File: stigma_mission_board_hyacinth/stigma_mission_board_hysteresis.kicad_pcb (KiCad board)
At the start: 4 copper layers, 50 x 150 mm, 207 parts, among them J1 Conn_02x04_Top_Bottom, J10 Conn_02x02_Top_Bottom, J11 Conn_02x02_Top_Bottom, J12 Conn_02x02_Top_Bottom, J13 Conn_02x02_Top_Bottom, J2 Conn_02x05_Top_Bottom_Mountin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, J3 Conn_02x04_Top_Bottom, J7 JST-GH 4Pin, J8 SMA, J9 SMA, Q1 DMN2056U, Q2 DMN2056U, Q3 AOSP21321, Q4 DMN2056U, Q5 AOSP21321, Q6 DMN2056U, Q7 AOSP21321, Q8 DMN2056U, Q9 AOSP21321, U1 L7805, U10 MCP2562-E-SN, U11 LAN8742A, U12 Ai-Thinker-Ra-01, U13 INA181, U14 INA181, U15 INA181, U16 INA181, U2 SN74HCS594, U3 L7805, U4 AZ1117H-ADJ, U5 INA181, U6 AZ1117H-ADJ, U7 MCP2562-E-SN, U8 Ai-Thinker-Ra-01, U9 TPD4E1U06, Y1 25MHz

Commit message: some tydiing up and adding footprints
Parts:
- added R59: 10k, Resistor_SMD:R_0603_1608Metric, F.Cu at (159.2, 130.5)
- added R60: 1k, Resistor_SMD:R_0603_1608Metric, F.Cu at (159.2, 133.0)
- JP3, JP4, JP5, JP6: footprint Jumper:SolderJumper-3_Open_RoundedPad2x2mm -> stigma:SolderJumper-3_Open_RoundedPad2x2mm
- R10: value 310R -> 100k; footprint Resistor_SMD:R_0402_1005Metric -> Resistor_SMD:R_0603_1608Metric
- R11: value 10k -> 220
- R12: value 10k -> 310R; footprint Resistor_SMD:R_0603_1608Metric -> Resistor_SMD:R_0402_1005Metric
- R14: value 150R -> 10k
- R15: value 220 -> 10k
- R16: value 310R -> 150R; footprint Resistor_SMD:R_0402_1005Metric -> Resistor_SMD:R_0603_1608Metric
- R17: value 0 -> 220; footprint Resistor_SMD:R_0402_1005Metric -> Resistor_SMD:R_0603_1608Metric
- R18: value 0 -> 310R
- R19: value 120, DNP -> 0; footprint Resistor_SMD:R_0603_1608Metric -> Resistor_SMD:R_0402_1005Metric
- R20: footprint Resistor_SMD:R_0603_1608Metric -> Resistor_SMD:R_0402_1005Metric
- R21: value 10k -> 120, DNP
- R22: value 1k5 -> 0
- R24: value 10k -> 1k5
- R26: value 120, DNP -> 10k
- R27: value 50R -> 10k
- R28: value 50R -> 120, DNP
- R31: value 0 -> 50R
- R32: value 33R -> 50R
- R33, R38: value 33R -> 0
- R34: value 10k -> 33R
- R36: value 0 -> 10k
- R37: value 12.1k -> 33R
- R39: value 10k -> 12.1k
- R4: value 150R -> 100k
- R40: value 270 -> 33R
- R41: value 270 -> 10k
- R42: value 10k -> 270
- R43: value 60R -> 270
- R44: value 1k -> 10k
- R45, R49, R53, R57: value 10k -> 60R
- R47, R51, R55: value 60R -> 10k
- R5: value @todo -> 10k
- R6: value 100mR 1% -> 150R; footprint Resistor_SMD:R_Shunt_Ohmite_LVK12 -> Resistor_SMD:R_0603_1608Metric
- R7: value 100k -> @todo
- R8: value 100k -> 100mR 1%; footprint Resistor_SMD:R_0603_1608Metric -> Resistor_SMD:R_Shunt_Ohmite_LVK12
- R9: value 220 -> 100k
- moved R40 241.0 mm to (273.9, 118.8)
- moved R42 241.0 mm to (273.9, 116.3)
- moved R41 231.3 mm to (274.0, 123.6)
- moved R17 205.6 mm to (272.2, 139.6)
- moved D14 191.2 mm to (193.0, 182.5)
- moved JP2 191.2 mm to (187.9, 179.7)
- moved JP3 186.4 mm to (152.0, 254.9)
- moved Q2 183.9 mm to (148.1, 269.2)
- moved R43 183.9 mm to (159.9, 261.2)
- moved U13 183.9 mm to (148.3, 264.5)
- moved C44 183.9 mm to (159.9, 251.2)
- moved D17 183.9 mm to (153.8, 269.0)
- moved D18 183.9 mm to (152.9, 266.0)
- moved D19 183.9 mm to (152.9, 263.4)
- moved Q3 183.9 mm to (166.1, 250.8)
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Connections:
- J4 pad 29: @TODO Free-ADC -> ADC_HIGH_CURRENT2
- R10 pad 1: Net-(U4-GND) -> high_current
- R10 pad 2: GND -> ADC_HIGH_CURRENT
- R11 pad 1: BUZZER -> Net-(D12-A)
- R11 pad 2: GND -> Net-(D13-A)
- R12 pad 1: ADC_MAIN_VOLTAGE -> Net-(U4-GND)
- R13 pad 1: ADC_HIGH_CURRENT -> BUZZER
- R14 pad 1: Net-(D15-A) -> ADC_MAIN_VOLTAGE
- R14 pad 2: Net-(U6-GND) -> GND
- R15 pad 1: Net-(D15-A) -> ADC_HIGH_CURRENT
- R15 pad 2: Net-(D16-A) -> GND
- R16 pad 1: Net-(U6-GND) -> Net-(D15-A)
- R16 pad 2: GND -> Net-(U6-GND)
- R17 pad 1: HSE_IN -> Net-(D15-A)
- R17 pad 2: Net-(C31-Pad2) -> Net-(D16-A)
- R18 pad 1: Net-(C32-Pad2) -> Net-(U6-GND)
- R18 pad 2: HSE_OUT -> GND
- R19 pad 1: CAN_1_H -> HSE_IN
- R19 pad 2: CAN_1_L -> Net-(C31-Pad2)
- R20 pad 1: Net-(U8-ANT) -> Net-(C32-Pad2)
- R20 pad 2: Net-(J8-In) -> HSE_OUT
- R21 pad 1: SR_ETH_RESET -> CAN_1_H
- R21 pad 2: +3.3V -> CAN_1_L
- R22 pad 1: Net-(U11-MDIO) -> Net-(U8-ANT)
- R22 pad 2: +3.3V -> Net-(J8-In)
- R23 pad 1: Net-(U11-CRS_DV/MODE2) -> SR_ETH_RESET
- R24 pad 1: Net-(U11-RXD1/MODE1) -> Net-(U11-MDIO)
- R25 pad 1: Net-(U11-RXD0/MODE0) -> Net-(U11-CRS_DV/MODE2)
- R26 pad 1: CAN_2_H -> Net-(U11-RXD1/MODE1)
- R26 pad 2: CAN_2_L -> +3.3V
- R27 pad 1: Net-(U11-VDD1A) -> Net-(U11-RXD0/MODE0)
- R27 pad 2: /TXP -> +3.3V
- R28 pad 1: Net-(U11-VDD1A) -> CAN_2_H
- R28 pad 2: /TXN -> CAN_2_L
- R29 pad 2: /RXP -> /TXP
- R30 pad 2: /RXN -> /TXN
- R31 pad 1: Net-(U12-ANT) -> Net-(U11-VDD1A)
- R31 pad 2: Net-(J9-In) -> /RXP
- R32 pad 1: Net-(U11-RXD0/MODE0) -> Net-(U11-VDD1A)
- R32 pad 2: ETH_RXD0 -> /RXN
- R33 pad 1: Net-(U11-RXD1/MODE1) -> Net-(U12-ANT)
- R33 pad 2: ETH_RXD1 -> Net-(J9-In)
- R34 pad 1: Net-(U11-RXER/PHYAD0) -> Net-(U11-RXD0/MODE0)
- R34 pad 2: GND -> ETH_RXD0
- R35 pad 1: Net-(U11-CRS_DV/MODE2) -> Net-(U11-RXD1/MODE1)
- R35 pad 2: ETH_RMII_CRS_DV -> ETH_RXD1
- R36 pad 1: Net-(U11-MDIO) -> Net-(U11-RXER/PHYAD0)
- R36 pad 2: ETH_MDIO -> GND
- R37 pad 1: Net-(U11-RBIAS) -> Net-(U11-CRS_DV/MODE2)
- R37 pad 2: GND -> ETH_RMII_CRS_DV
- R38 pad 1: Net-(U11-~{INT}/REFCLKO) -> Net-(U11-MDIO)
- R38 pad 2: ETH_REF_CLK -> ETH_MDIO
- R39 pad 1: ETH_nINT -> Net-(U11-RBIAS)
- R4 pad 1: Net-(D12-A) -> high_current
- R4 pad 2: Net-(U4-GND) -> ADC_HIGH_CURRENT2
- R40 pad 1: Net-(RJ1-L-) -> Net-(U11-~{INT}/REFCLKO)
- R40 pad 2: GND -> ETH_REF_CLK
- R41 pad 1: Net-(RJ1-R+) -> ETH_nINT
- R42 pad 1: +3.3V -> Net-(RJ1-L-)
- R42 pad 2: ETH_nINT -> GND
- R43 pad 1: RECOVERY_3_CONT_CHECK -> Net-(RJ1-R+)
- R43 pad 2: Net-(U13-+) -> GND
- R44 pad 1: /Recovery Output3/high_current -> +3.3V
- R44 pad 2: Net-(Q2-D) -> ETH_nINT
- R45 pad 1: RECOVERY_3 -> RECOVERY_3_CONT_CHECK
- R45 pad 2: GND -> Net-(U13-+)
- R46 pad 1: /Recovery Output3/recovery_switched -> /Recovery Output3/high_current
- R46 pad 2: Net-(D19-A) -> Net-(Q2-D)
- R47 pad 1: RECOVERY_2_CONT_CHECK -> RECOVERY_3
- R47 pad 2: Net-(U14-+) -> GND
- R48 pad 1: /Recovery Output2/high_current -> /Recovery Output3/recovery_switched
- R48 pad 2: Net-(Q4-D) -> Net-(D19-A)
- R49 pad 1: RECOVERY_2 -> RECOVERY_2_CONT_CHECK
- R49 pad 2: GND -> Net-(U14-+)
- R5 pad 1: BUZZER -> ADC_HIGH_CURRENT2
- R5 pad 2: Net-(Q1-G) -> GND
- R50 pad 1: /Recovery Output2/recovery_switched -> /Recovery Output2/high_current
- R50 pad 2: Net-(D22-A) -> Net-(Q4-D)
- R51 pad 1: RECOVERY_4_CONT_CHECK -> RECOVERY_2
- R51 pad 2: Net-(U15-+) -> GND
- R52 pad 1: /Recovery Output 4/high_current -> /Recovery Output2/recovery_switched
- R52 pad 2: Net-(Q6-D) -> Net-(D22-A)
- R53 pad 1: RECOVERY_4 -> RECOVERY_4_CONT_CHECK
- R53 pad 2: GND -> Net-(U15-+)
- R54 pad 1: /Recovery Output 4/recovery_switched -> /Recovery Output 4/high_current
- R54 pad 2: Net-(D25-A) -> Net-(Q6-D)
- R55 pad 1: RECOVERY_1_CONT_CHECK -> RECOVERY_4
- R55 pad 2: Net-(U16-+) -> GND
- R56 pad 1: /Recovery Output 1/high_current -> /Recovery Output 4/recovery_switched
- R56 pad 2: Net-(Q8-D) -> Net-(D25-A)
- R57 pad 1: RECOVERY_1 -> RECOVERY_1_CONT_CHECK
- R57 pad 2: GND -> Net-(U16-+)
- R58 pad 1: /Recovery Output 1/recovery_switched -> /Recovery Output 1/high_current
- R58 pad 2: Net-(D28-A) -> Net-(Q8-D)
- R6 pad 1: v_main_pre_sense -> Net-(D12-A)
- R6 pad 2: Net-(U5-+) -> Net-(U4-GND)
- R7 pad 1: v_main_pre_sense -> BUZZER
- R7 pad 2: ADC_MAIN_VOLTAGE -> Net-(Q1-G)
- R8 pad 1: high_current -> v_main_pre_sense
- R8 pad 2: ADC_HIGH_CURRENT -> Net-(U5-+)
- R9 pad 1: Net-(D12-A) -> v_main_pre_sense
- R9 pad 2: Net-(D13-A) -> ADC_MAIN_VOLTAGE
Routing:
- net Net-(U15-+): vias 1 -> 0
- net GND: vias 24 -> 11
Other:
- board text added: "recovery1"
- board text added: "recovery2"
- board text added: "recovery3"
- board text added: "recovery4"
- board text added: "see what we do with those"
- board text removed: "50 x 200 mm"
- board text removed: "R1"
- board text removed: "R2"
- board text removed: "R3"
- board text removed: "R4"
- board text removed: "Recovery Power 1"
- board text removed: "Recovery Power 2"
- board text removed: "Vehicle BUS"

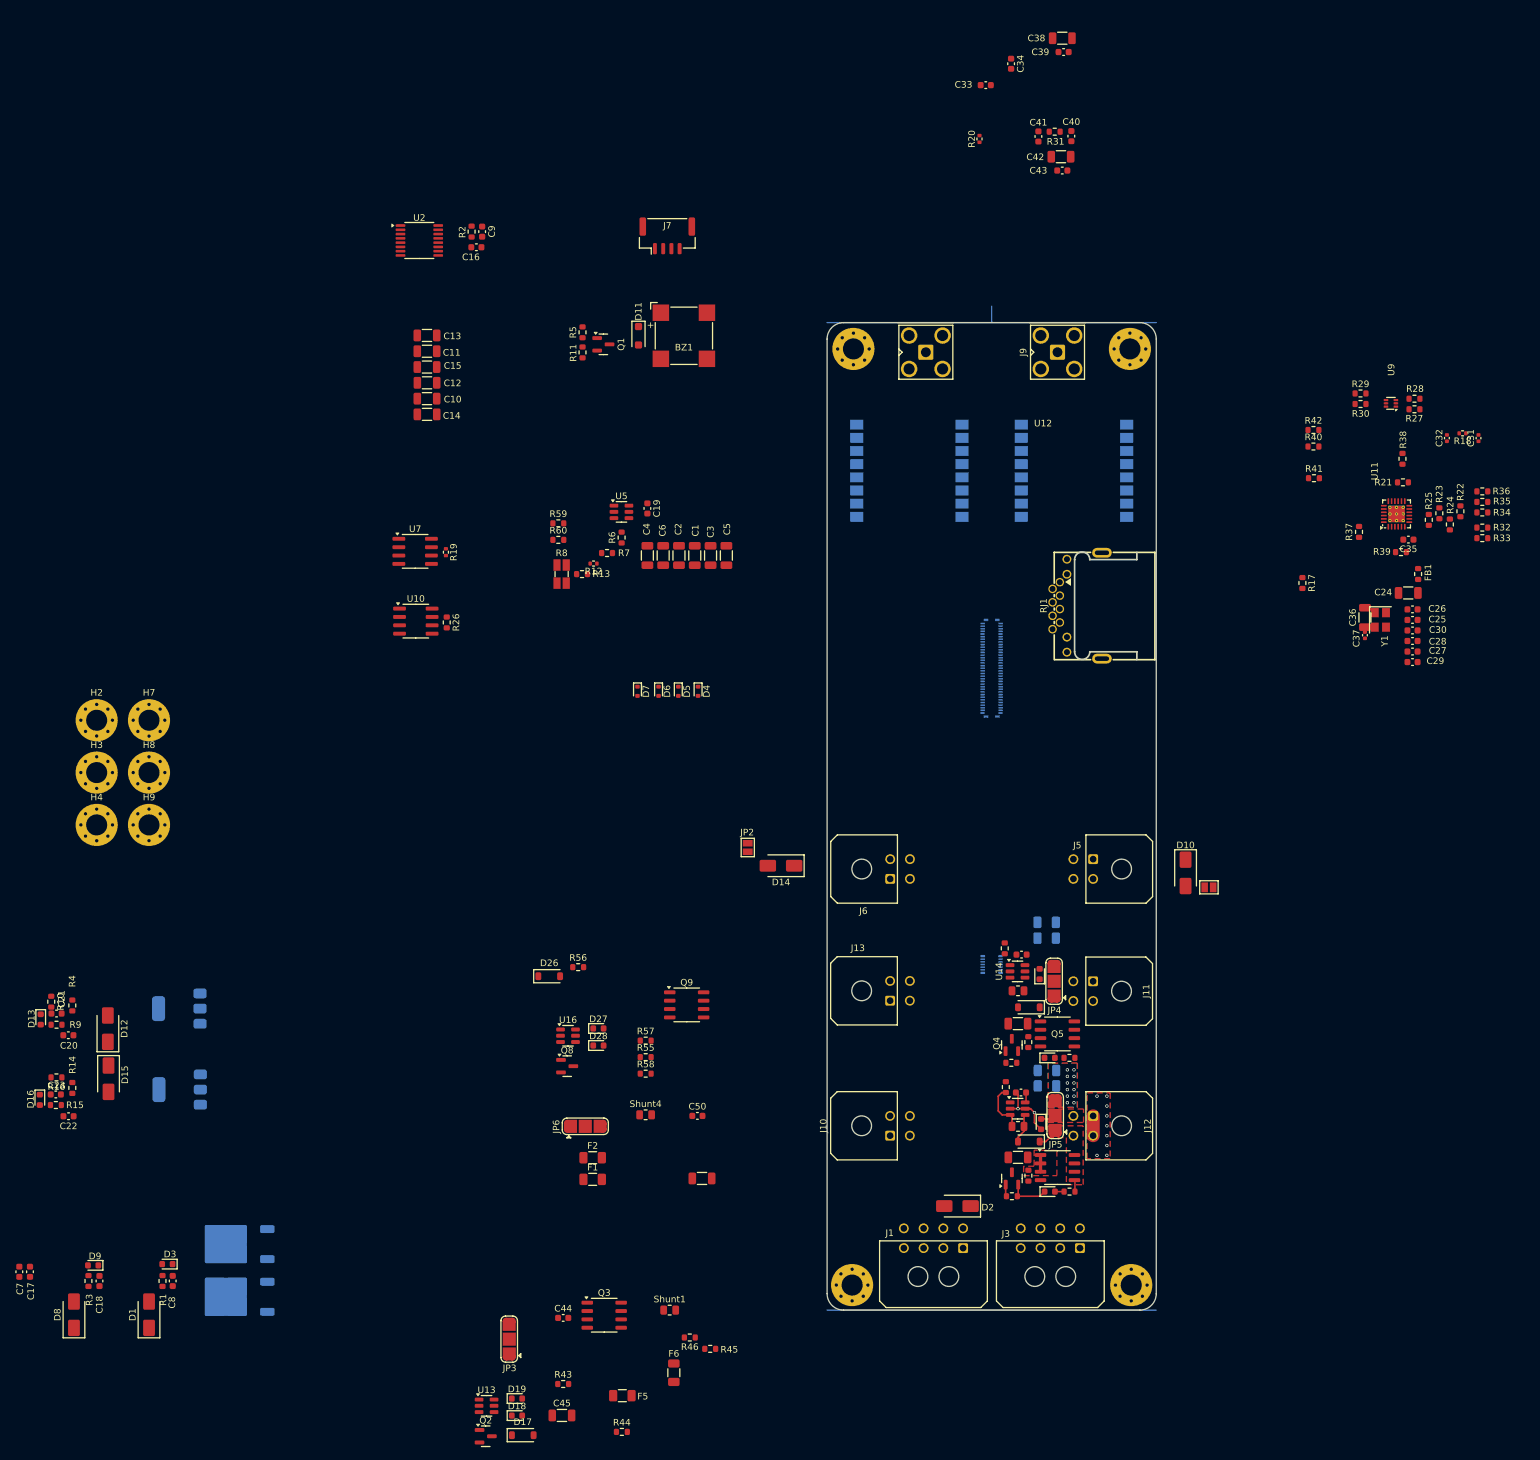
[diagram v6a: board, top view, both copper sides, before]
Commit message: added the other 2 recovery outputs and sorted all components
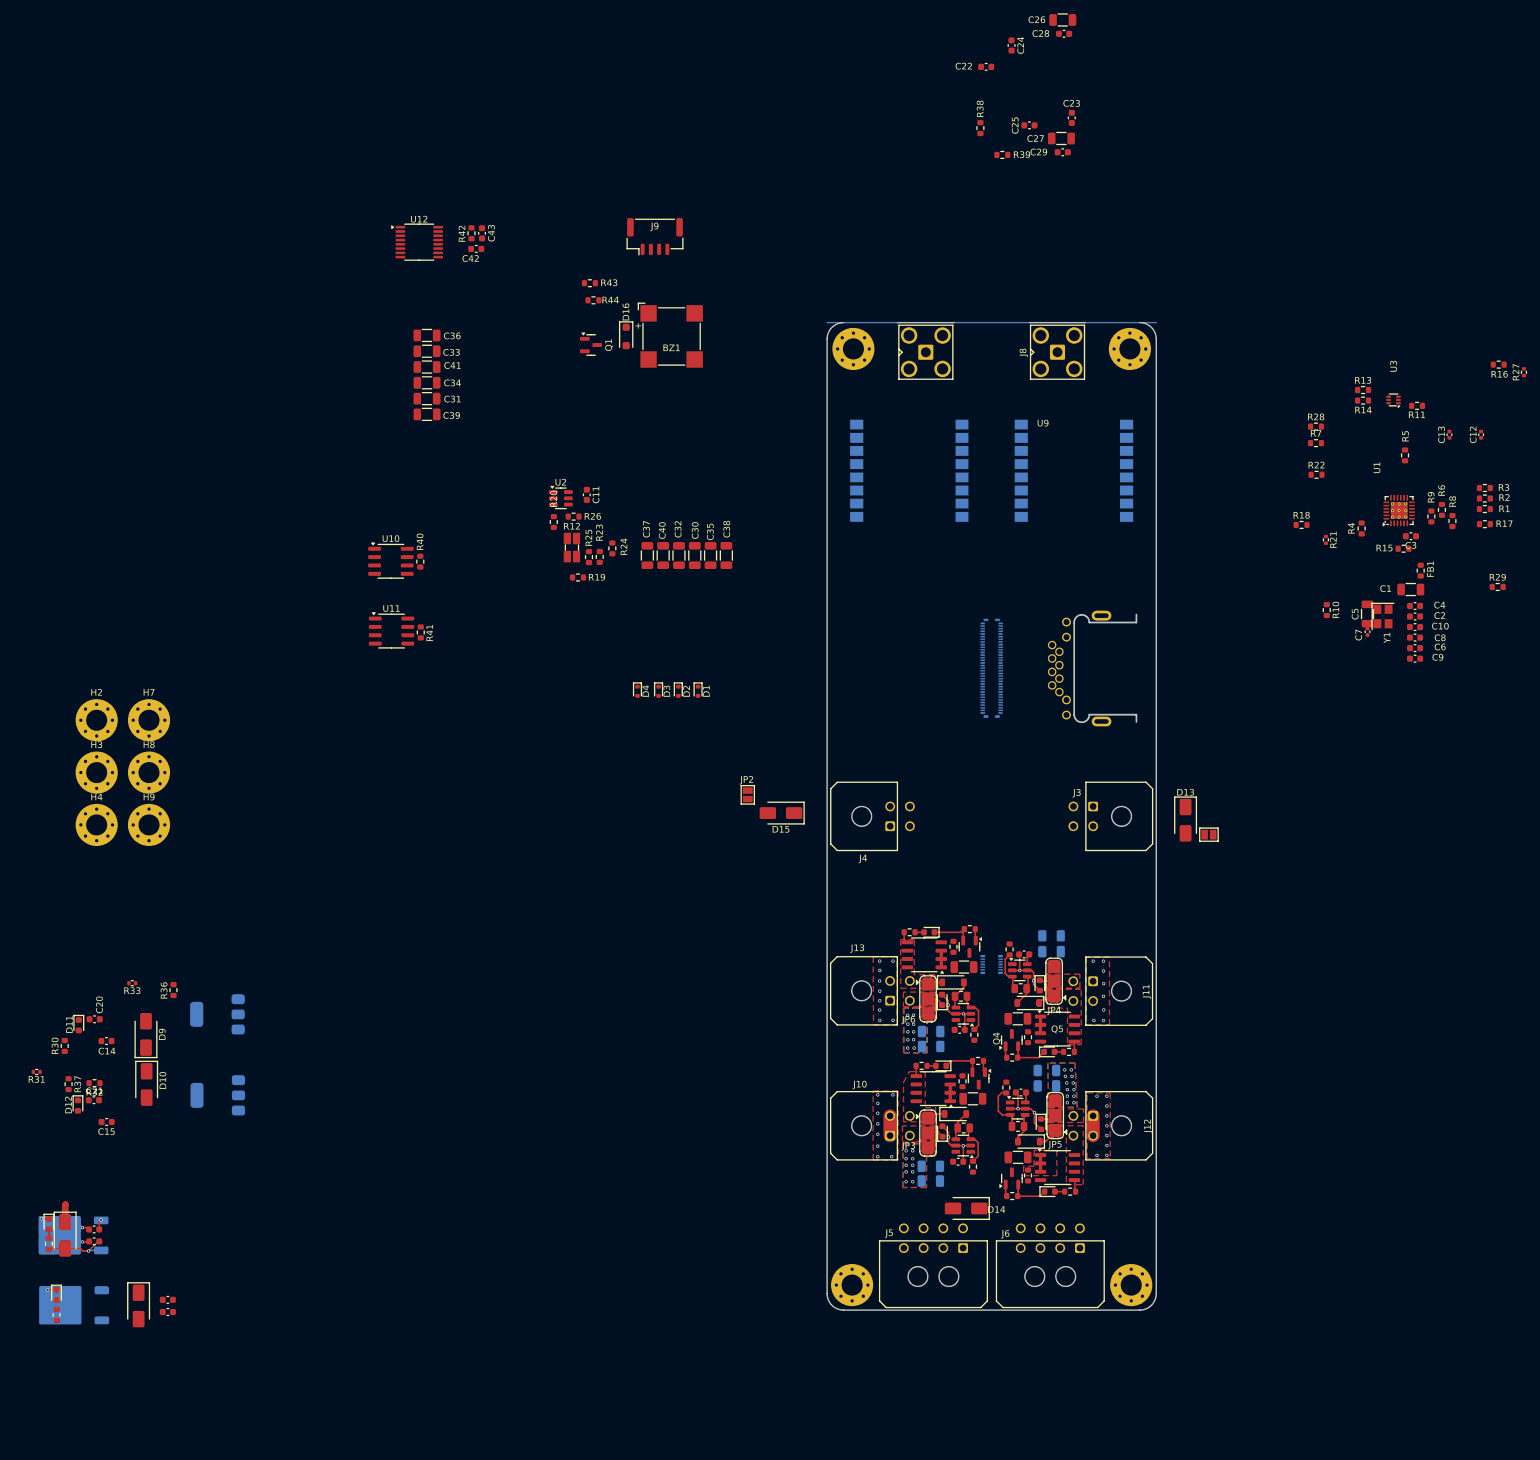
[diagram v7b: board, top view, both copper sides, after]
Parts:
- F1: moved to B.Cu
- F2: renamed from F5; moved to B.Cu
- F3: renamed from F2; moved to B.Cu
- F4: renamed from F6; moved to B.Cu
- J2: footprint stigma:DF40GB-10DP-0.4V-plug -> Stigma:DF40GB-10DP-0.4V-plug
- JP3, JP4, JP5, JP6: footprint stigma:SolderJumper-3_Open_RoundedPad2x2mm -> Stigma:SolderJumper-3_Open_RoundedPad2x2mm
- RJ1: footprint stigma:RJ45-TH_MJ88B-B011-RVL11-P -> Stigma:RJ45-TH_MJ88B-B011-RVL11-P; moved to B.Cu
- moved R33 218.6 mm to (94.5, 200.3)
- moved R37 202.3 mm to (84.8, 215.7)
- moved R29 186.6 mm to (301.9, 140.2)
- moved R18 172.2 mm to (272.1, 130.7)
- moved R41 155.1 mm to (138.3, 147.1), turned to -90 degrees
- moved R40 149.7 mm to (138.2, 136.3), turned to -90 degrees
- moved R10 133.7 mm to (275.9, 143.7)
- moved R21 133.7 mm to (275.8, 133.0)
- moved R26 119.1 mm to (161.5, 129.5)
- moved R36 115.1 mm to (100.7, 201.4)
- moved R31 114.5 mm to (79.9, 213.8)
- moved R30 114.5 mm to (84.2, 209.9)
- moved R20 112.9 mm to (158.5, 130.3)
- moved R25 106.0 mm to (163.8, 135.6)
- moved R23 105.2 mm to (165.5, 135.6)
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- renumbered C24 to C1, C30 to C10, C19 to C11, C31 to C12, C32 to C13, C20 to C14, C22 to C15, C7 to C16, C8 to C18, C18 to C19, C25 to C2, C21 to C20, C23 to C21, C33 to C22, C40 to C23, C34 to C24, C41 to C25, C38 to C26, C42 to C27, C39 to C28, C43 to C29, C35 to C3, C1 to C30, C10 to C31, C2 to C32, C11 to C33, C12 to C34, C3 to C35, C13 to C36, C4 to C37, C5 to C38, C14 to C39, C26 to C4, C6 to C40, C15 to C41, C16 to C42, C9 to C43, C45 to C44, C44 to C45, C47 to C46, C46 to C47, C49 to C48, C48 to C49, C36 to C5, C51 to C50, C50 to C51, C27 to C6, C37 to C7, C28 to C8, C29 to C9, D4 to D1, D15 to D10, D13 to D11, D16 to D12, D10 to D13, D2 to D14, D14 to D15, D11 to D16, D19 to D18, D18 to D19, D5 to D2, D22 to D21, D21 to D22, D25 to D24, D24 to D25, D28 to D27, D27 to D28, D6 to D3, D7 to D4, D1 to D5, D8 to D6, D3 to D7, D9 to D8, D12 to D9, F3 to F5, F4 to F6, J4 to J1, J5 to J3, J6 to J4, J1 to J5, J3 to J6, J8 to J7, J9 to J8, J7 to J9, R34 to R1, R26 to R10, R27 to R11, R8 to R12, R29 to R13, R30 to R14, R39 to R15, R31 to R16, R32 to R17, R44 to R18, R9 to R19, R35 to R2, R14 to R20, R19 to R21, R41 to R22, R4 to R23, R5 to R24, R10 to R25, R15 to R26, R20 to R27, R42 to R28, R43 to R29, R36 to R3, R6 to R30, R12 to R31, R16 to R32, R18 to R33, R1 to R34, R3 to R35, R11 to R36, R17 to R37, R22 to R38, R33 to R39, R37 to R4, R21 to R40, R28 to R41, R2 to R42, R13 to R43, R7 to R44, R47 to R45, R45 to R47, R51 to R49, R38 to R5, R49 to R51, R55 to R53, R53 to R55, R59 to R57, R57 to R59, R23 to R6, R40 to R7, R24 to R8, R25 to R9, U11 to U1, U7 to U10, U10 to U11, U2 to U12, U5 to U2, U9 to U3, U1 to U4, U3 to U5, U4 to U6, U6 to U7, U12 to U9
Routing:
- net GND: track 19.2 -> 76.8 mm, vias 11 -> 47
- net Net-(D5-A): track 0.00 -> 10.4 mm, vias 0 -> 1
- net Net-(U13-+): track 0.00 -> 6.92 mm
- net Net-(U16-+): track 0.00 -> 6.41 mm
- net Net-(U14-+): track 0.00 -> 6.38 mm
- net Net-(D20-A): track 0.00 -> 4.93 mm
- net Net-(D17-A): track 0.00 -> 4.50 mm
- net Net-(D26-A): track 0.00 -> 4.44 mm
- net /Recovery Output2/recovery_switched: track 0.00 -> 4.18 mm
- net /Recovery Output 1/recovery_switched: track 0.00 -> 3.87 mm
- net /Recovery Output3/recovery_switched: track 0.00 -> 3.82 mm
- net +5V: track 0.00 -> 2.72 mm
- net /Recovery Output 1/servo_line: track 0.00 -> 2.63 mm
- net /Recovery Output3/high_current: track 0.00 -> 2.54 mm, vias 0 -> 10
- net /Recovery Output2/high_current: track 0.00 -> 2.54 mm
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- added copper zone on B.Cu, net /Recovery Output 1/high_current
- added copper zone on F.Cu, net /Recovery Output 1/high_current
- added copper zone on F.Cu, net /Recovery Output 1/recovery_switched
- added copper zone on F.Cu, net /Recovery Output 1/servo_line
- added copper zone on F.Cu, net /Recovery Output2/recovery_switched
- added copper zone on F.Cu, net /Recovery Output2/servo_line
- added copper zone on B.Cu, net /Recovery Output3/high_current
- added copper zone on F.Cu, net /Recovery Output3/high_current
- added copper zone on F.Cu, net /Recovery Output3/recovery_switched
- added copper zone on F.Cu, net /Recovery Output3/servo_line
